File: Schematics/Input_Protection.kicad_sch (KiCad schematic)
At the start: 6 parts, among them Q1 STB10NK60ZT4

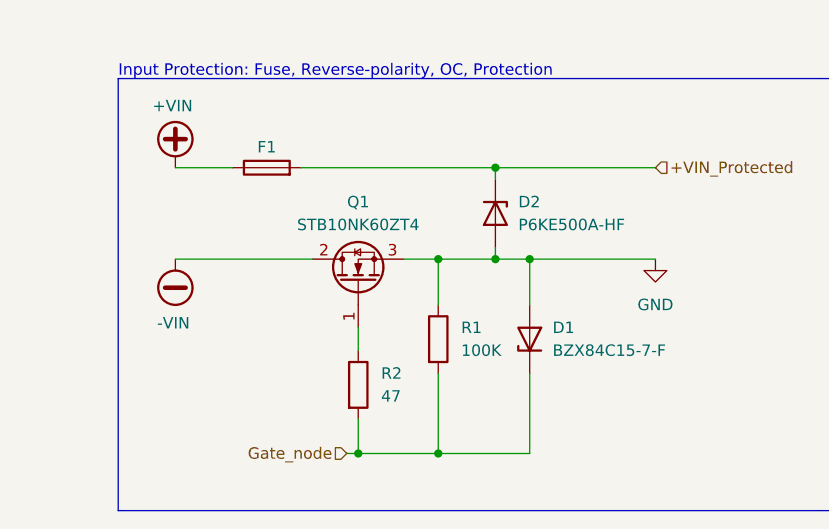
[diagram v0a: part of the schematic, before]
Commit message: [WIP - SIC Inverter]
- Added 3d models for 3 parts
- Added 3 new footprints for the 3 added parts
- Changed footprint 23AH8785 and 86 Black and Red
- Finished WIP with EMI, Input Protection, and Precharge
- Added datasheet
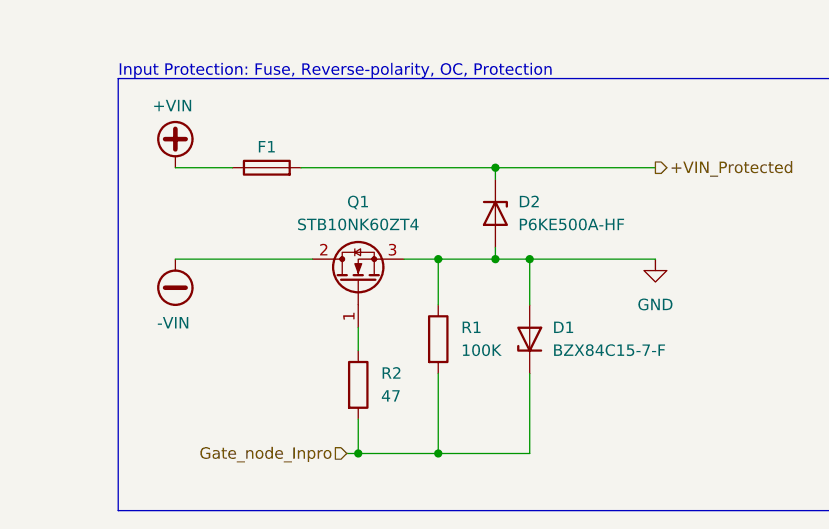
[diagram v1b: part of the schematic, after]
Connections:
- net Gate_node renamed Gate_node_Inpro
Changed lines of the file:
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@@
 	)
 	(hierarchical_label "+VIN_Protected"
-		(shape input)
+		(shape output)
 		(at 170.18 91.44 0)
 		(effects
@@
 		)
 	)
-	(hierarchical_label "Gate_node"
+	(hierarchical_label "Gate_node_Inpro"
 		(shape input)
 		(at 135.89 123.19 180)

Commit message: [WIP Full Bridge Leg A High Side]
- Changed Footprint for Black and Red connectors to THP but no Pin
  number
- Changed DC Link cap sub sheet to have a cleaner look
- Change footprint in 1206 reister to head solder pads
- WIP Full Bridge Leg A High Side
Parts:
- R1, R2: footprint Resistor_SMD:R_1206_3216Metric -> Resistor_SMD:R_1206_3216Metric_Pad1.30x1.75mm_HandSolder
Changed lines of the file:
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@@
 			)
 		)
-		(property "Footprint" "Resistor_SMD:R_1206_3216Metric"
+		(property "Footprint" "Resistor_SMD:R_1206_3216Metric_Pad1.30x1.75mm_HandSolder"
 			(at 144.272 110.49 90)
 			(effects
@@
 			)
 		)
-		(property "Footprint" "Resistor_SMD:R_1206_3216Metric"
+		(property "Footprint" "Resistor_SMD:R_1206_3216Metric_Pad1.30x1.75mm_HandSolder"
 			(at 135.382 115.57 90)
 			(effects

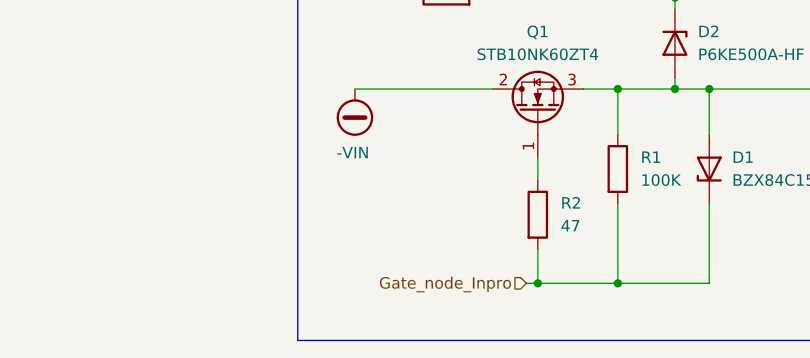
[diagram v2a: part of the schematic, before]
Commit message: [WIP SiC Single Phase Inverter
- Updated README.md
- Added New Parts for Output filter L,C,R
- Added datasheets for the new parts
- Added 3D models for the new parts
- Added new symbols and footprints for the L,C,R
- Finished output filter
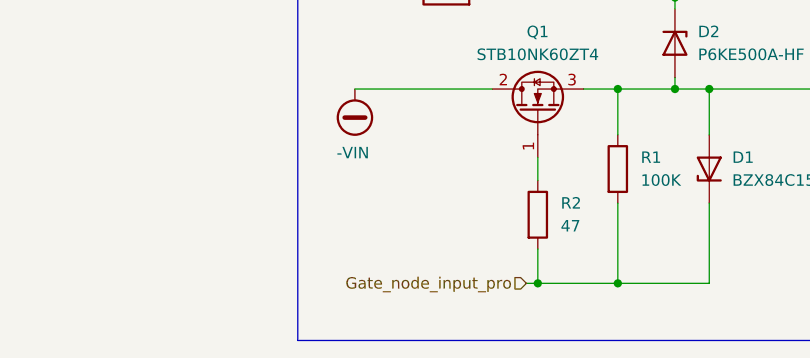
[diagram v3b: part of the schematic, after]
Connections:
- net Gate_node_Inpro renamed Gate_node_input_pro
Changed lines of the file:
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@@
 		)
 	)
-	(hierarchical_label "Gate_node_Inpro"
+	(hierarchical_label "Gate_node_input_pro"
 		(shape input)
 		(at 135.89 123.19 180)

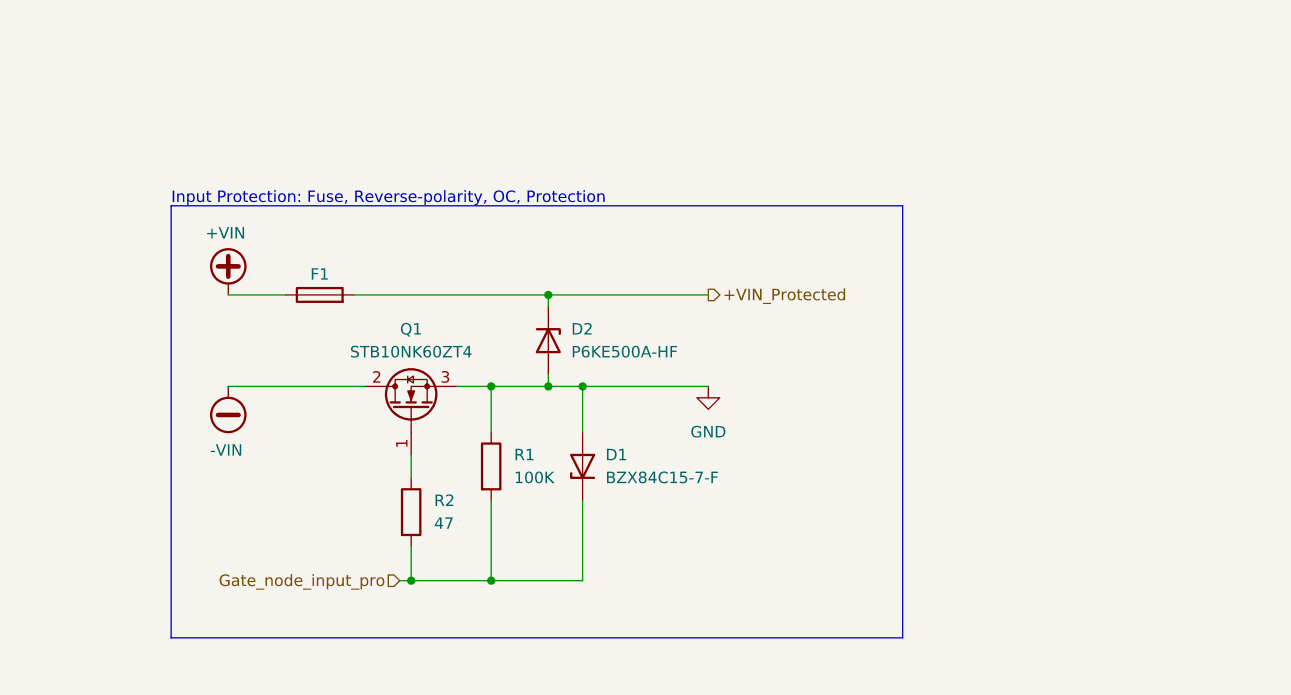
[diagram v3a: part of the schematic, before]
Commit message: [WIP SiC Single Phase Inverter]
- Added PCB to PCB Male and Female connectors
- Added symbols, footprints and 3d models for the parts listed above
- Added Male and Female connectors to input protection and input emi
  subsheets
- Changed PCB editor to account for two edge cuts/ two sub circuits
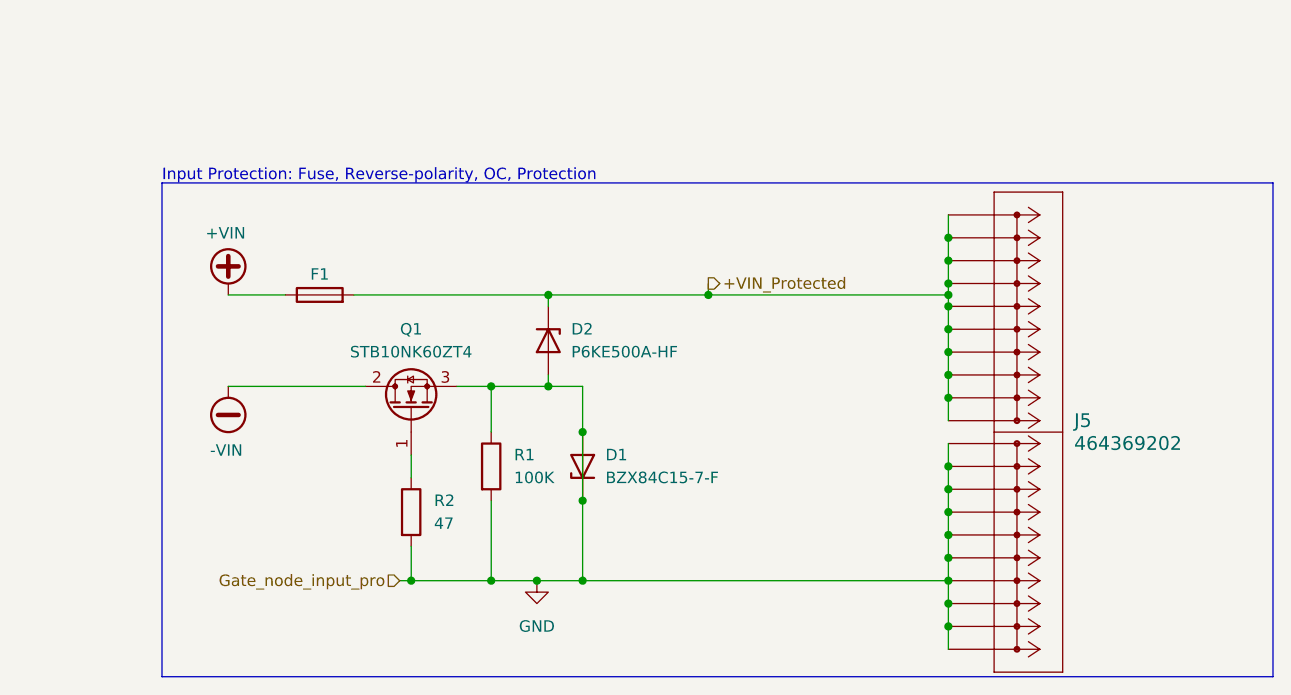
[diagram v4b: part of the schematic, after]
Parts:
- added J5: 464369202, SiC_Inverter:46436-900_02, symbol SiC_Inverter:464369202
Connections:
- net Gate_node_input_pro is gone; now on net GND: D1.1 (K), R1.2, R2.2
- net +VIN_Protected: now also J5.P1_1, J5.P1_10, J5.P1_2, J5.P1_3, J5.P1_4, J5.P1_5, J5.P1_6, J5.P1_7, J5.P1_8, J5.P1_9
- net GND: now also J5.P2_1, J5.P2_10, J5.P2_2, J5.P2_3, J5.P2_4, J5.P2_5, J5.P2_6, J5.P2_7, J5.P2_8, J5.P2_9

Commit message: Changing Text to Text Block
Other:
- note removed: "Input Protection: Fuse, Reverse-polarity, OC, Protection"
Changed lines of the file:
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@@
-		)
-	)
-	(text "Input Protection: Fuse, Reverse-polarity, OC, Protection\n"
-		(exclude_from_sim no)
-		(at 109.474 78.232 0)
-		(effects
-			(font
-				(size 1.27 1.27)
-			)
-			(justify left)
 		)
 	)
@@
 		)
 	)
+	(text_box "Input Protection: Fuse, Reverse-polarity, OC, Protection\n"
+		(exclude_from_sim no)
+		(at 109.474 75.692 0)
+		(size 56.896 3.048)
+		(margins 0.9525 0.9525 0.9525 0.9525)
+		(stroke
+			(width 0)
+			(type solid)
+		)
+		(fill
+			(type color)
+			(color 0 0 255 0.1)
+		)
+		(effects
+			(font
+				(size 1.27 1.27)
+			)
+			(justify left top)
+		)
+	)

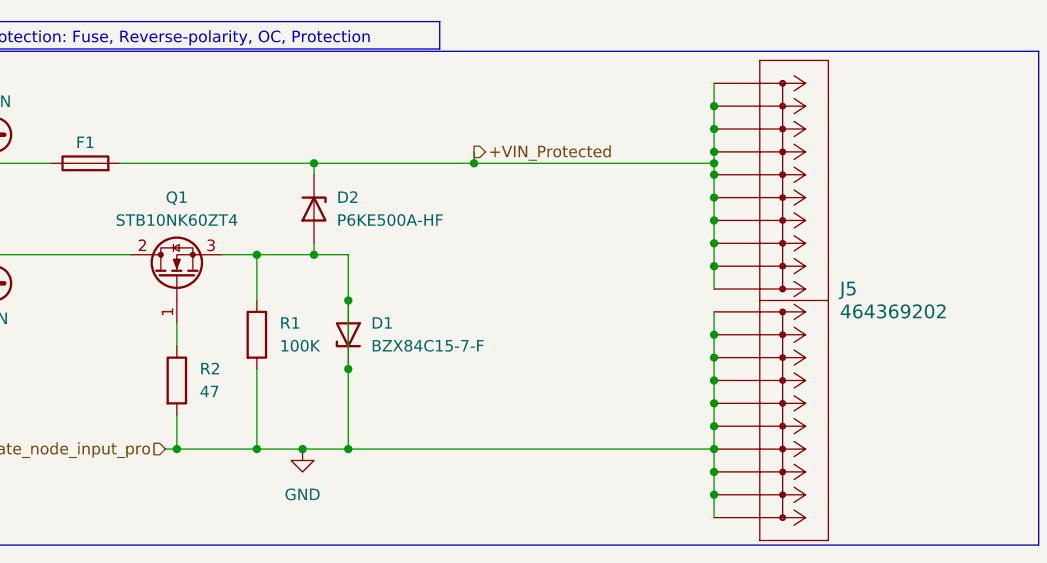
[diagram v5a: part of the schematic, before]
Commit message: [WIP Single Phase Inverter]
- Changed all Refs within each sub sheet (Stripe)
- Added 3V3 Power Supply off of 15V iso supply
- Added footprint, symbol and 3d part
- updated PCB with new part
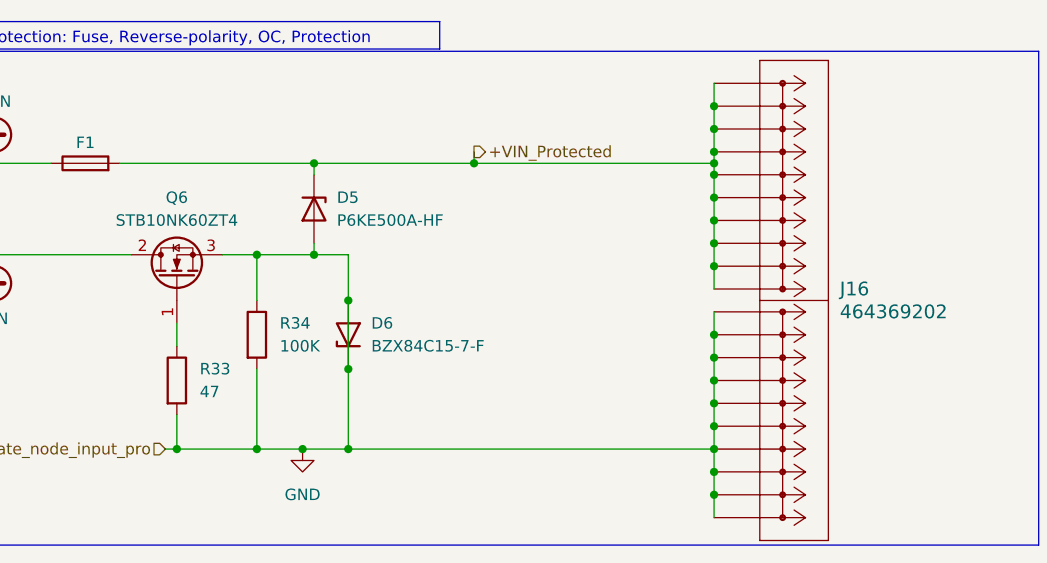
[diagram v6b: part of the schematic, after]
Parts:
- renumbered D2 to D5, D1 to D6, J5 to J16, Q1 to Q6, R2 to R33, R1 to R34
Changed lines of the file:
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@@
 		(dnp no)
 		(fields_autoplaced yes)
-		(property "Reference" "D1"
+		(property "Reference" "D6"
 			(at 158.75 109.2199 90)
 			(effects
@@
 			(project ""
 				(path "/a1ed0539-9735-4ad1-a8fd-87e26e7fce16/cf3acd45-2ee3-4687-9429-99700ff01ea1"
-					(reference "D1")
+					(reference "D6")
 					(unit 1)
 				)
@@
 		(on_board yes)
 		(dnp no)
-		(property "Reference" "#PWR02"
+		(property "Reference" "#PWR082"
 			(at 116.84 93.98 0)
 			(effects
@@
 			(project "SiC_Single_Phase_Inverter"
 				(path "/a1ed0539-9735-4ad1-a8fd-87e26e7fce16/cf3acd45-2ee3-4687-9429-99700ff01ea1"
-					(reference "#PWR02")
+					(reference "#PWR082")
 					(unit 1)
 				)
@@
 		(dnp no)
 		(fields_autoplaced yes)
-		(property "Reference" "D2"
+		(property "Reference" "D5"
 			(at 154.94 95.2499 90)
 			(effects
@@
 			(project ""
 				(path "/a1ed0539-9735-4ad1-a8fd-87e26e7fce16/cf3acd45-2ee3-4687-9429-99700ff01ea1"
-					(reference "D2")
+					(reference "D5")
 					(unit 1)
 				)
@@
 		(dnp no)
 		(fields_autoplaced yes)
-		(property "Reference" "Q1"
+		(property "Reference" "Q6"
 			(at 137.16 95.25 90)
 			(effects
@@
 			(project ""
 				(path "/a1ed0539-9735-4ad1-a8fd-87e26e7fce16/cf3acd45-2ee3-4687-9429-99700ff01ea1"
-					(reference "Q1")
+					(reference "Q6")
 					(unit 1)
 				)
@@
 		(dnp no)
 		(fields_autoplaced yes)
-		(property "Reference" "R1"
+		(property "Reference" "R34"
 			(at 148.59 109.2199 0)
 			(effects
@@
 			(project ""
 				(path "/a1ed0539-9735-4ad1-a8fd-87e26e7fce16/cf3acd45-2ee3-4687-9429-99700ff01ea1"
-					(reference "R1")
+					(reference "R34")
 					(unit 1)
 				)
@@
 		(dnp no)
 		(fields_autoplaced yes)
-		(property "Reference" "J5"
+		(property "Reference" "J16"
 			(at 210.82 105.4099 0)
 			(effects
@@
 			(project ""
 				(path "/a1ed0539-9735-4ad1-a8fd-87e26e7fce16/cf3acd45-2ee3-4687-9429-99700ff01ea1"
-					(reference "J5")
+					(reference "J16")
 					(unit 1)
 				)
@@
 		(on_board yes)
 		(dnp no)
-		(property "Reference" "#PWR06"
+		(property "Reference" "#PWR083"
 			(at 116.84 99.06 0)
 			(effects
@@
 			(project "SiC_Single_Phase_Inverter"
 				(path "/a1ed0539-9735-4ad1-a8fd-87e26e7fce16/cf3acd45-2ee3-4687-9429-99700ff01ea1"
-					(reference "#PWR06")
+					(reference "#PWR083")
 					(unit 1)
 				)
@@
 		(dnp no)
 		(fields_autoplaced yes)
-		(property "Reference" "#PWR03"
+		(property "Reference" "#PWR084"
 			(at 151.13 129.54 0)
 			(effects
@@
 			(project ""
 				(path "/a1ed0539-9735-4ad1-a8fd-87e26e7fce16/cf3acd45-2ee3-4687-9429-99700ff01ea1"
-					(reference "#PWR03")
+					(reference "#PWR084")
 					(unit 1)
 				)
@@
 		(dnp no)
 		(fields_autoplaced yes)
-		(property "Reference" "R2"
+		(property "Reference" "R33"
 			(at 139.7 114.2999 0)
 			(effects
@@
 			(project ""
 				(path "/a1ed0539-9735-4ad1-a8fd-87e26e7fce16/cf3acd45-2ee3-4687-9429-99700ff01ea1"
-					(reference "R2")
-					(unit 1)
-				)
+					(reference "R33")
+					(unit 1)
+				)

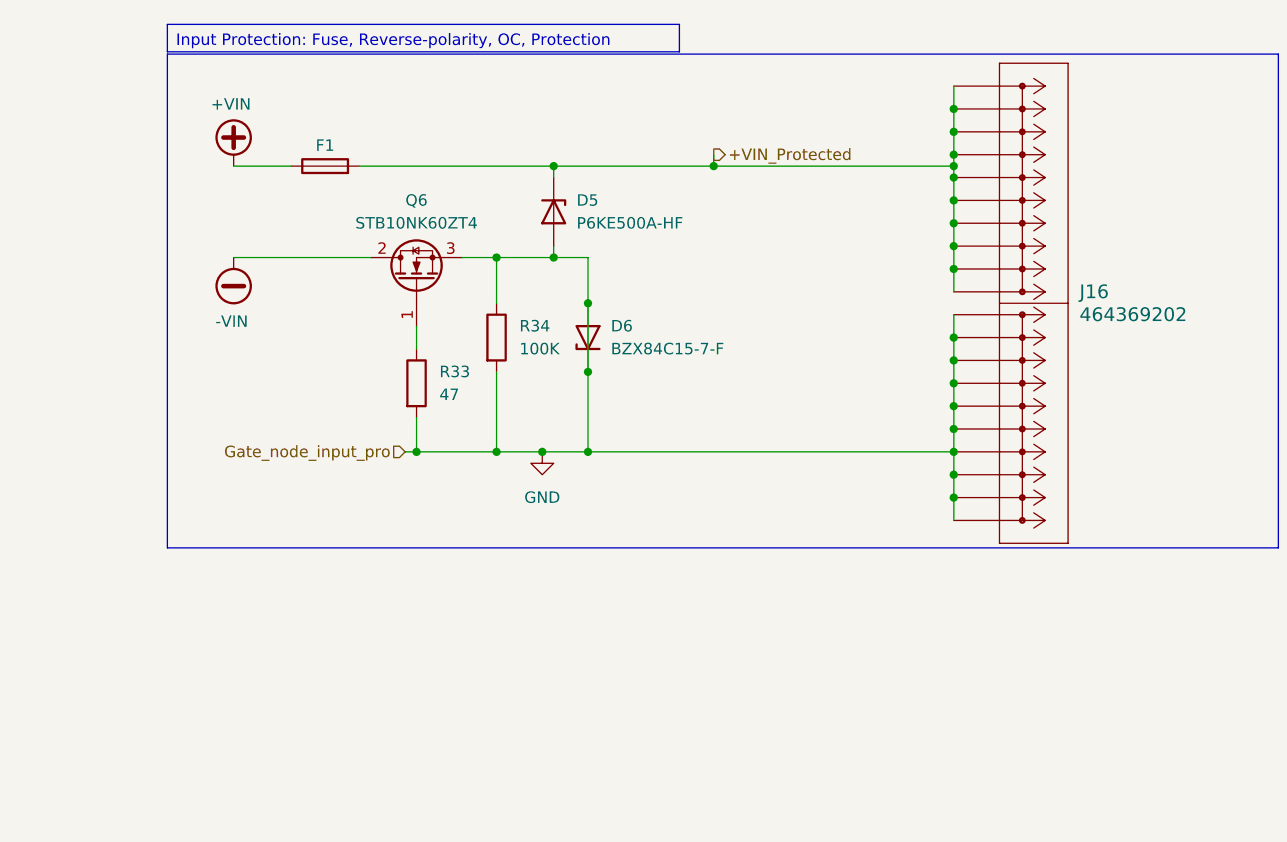
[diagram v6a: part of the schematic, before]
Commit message: [Milestone Compelted Controller and USB]
- Added Test Points
- Completed USB circuit to Controller
- Wired up Controller
- Added Connectors to Power Subsheet and 12pin from cotnroller to Full
  Bridge
- Added 3d models for USB compoents
- General fixes to subsheets
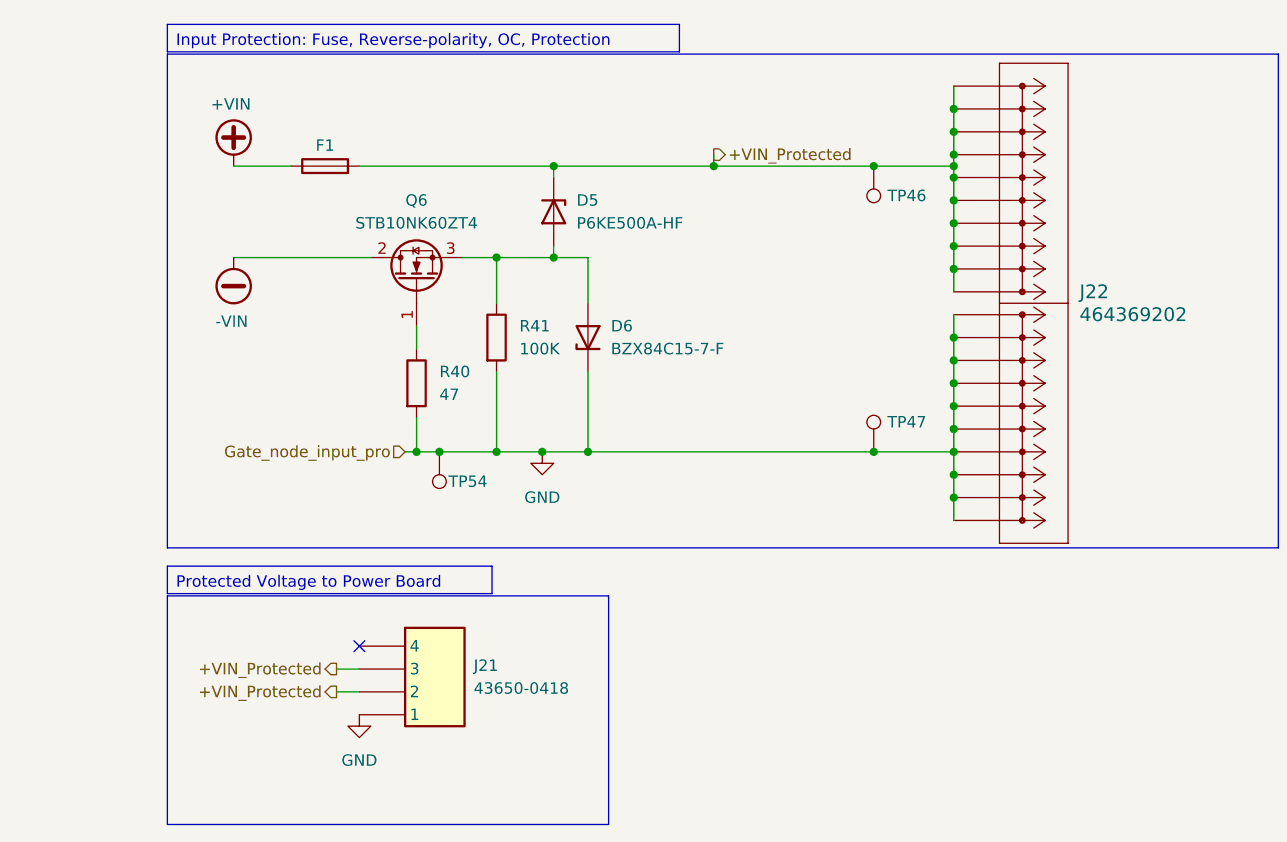
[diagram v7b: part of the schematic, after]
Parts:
- added J21: 43650-0418, SiC_Inverter:436500418, symbol SiC_Inverter:43650-0418
- added TP46, TP54: 5277, SiC_Inverter:5277, symbol SiC_Inverter:5277
- added TP47: 5281, SiC_Inverter:5281, symbol SiC_Inverter:5281
- renumbered J16 to J22, R33 to R40, R34 to R41
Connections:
- net +VIN_Protected: now also J21.2, J21.3, TP46.1
- net GND: now also J21.1, TP47.1, TP54.1; no longer D5.2 (A), D6.2 (A), Q6.3, R41.1
- new net: D5.2 (A), D6.2 (A), Q6.3, R41.1
- no-connect marks 0 -> 1
